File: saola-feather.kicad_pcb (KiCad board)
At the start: 2 copper layers, 27.9 x 53.3 mm, 11 parts, among them J1 Conn_01x21_Female, J2 FeatherTop, J3 Conn_01x04_Male, J4 USB_B_Micro, J5 FeatherBottom, J6 Conn_02x05_Odd_Even, J7 Conn_01x21_Female

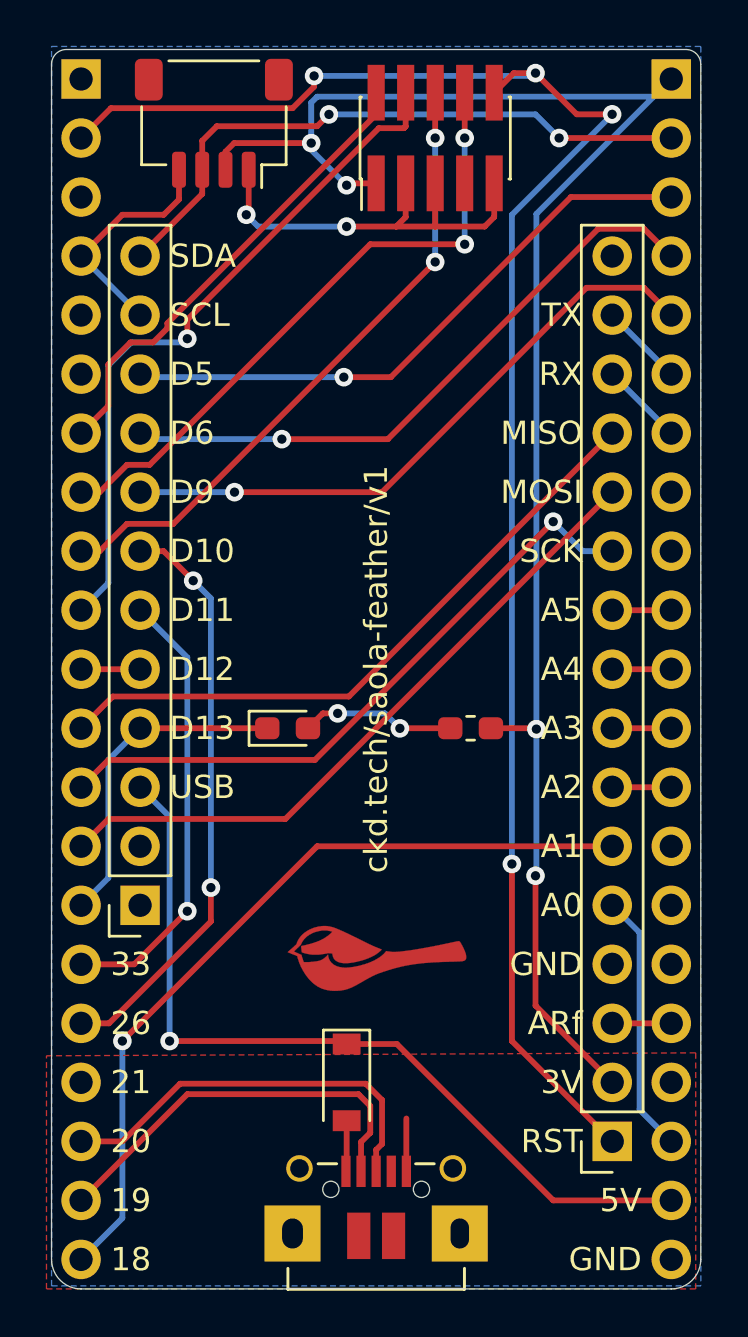
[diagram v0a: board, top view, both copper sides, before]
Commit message: Second version with fixed I2C
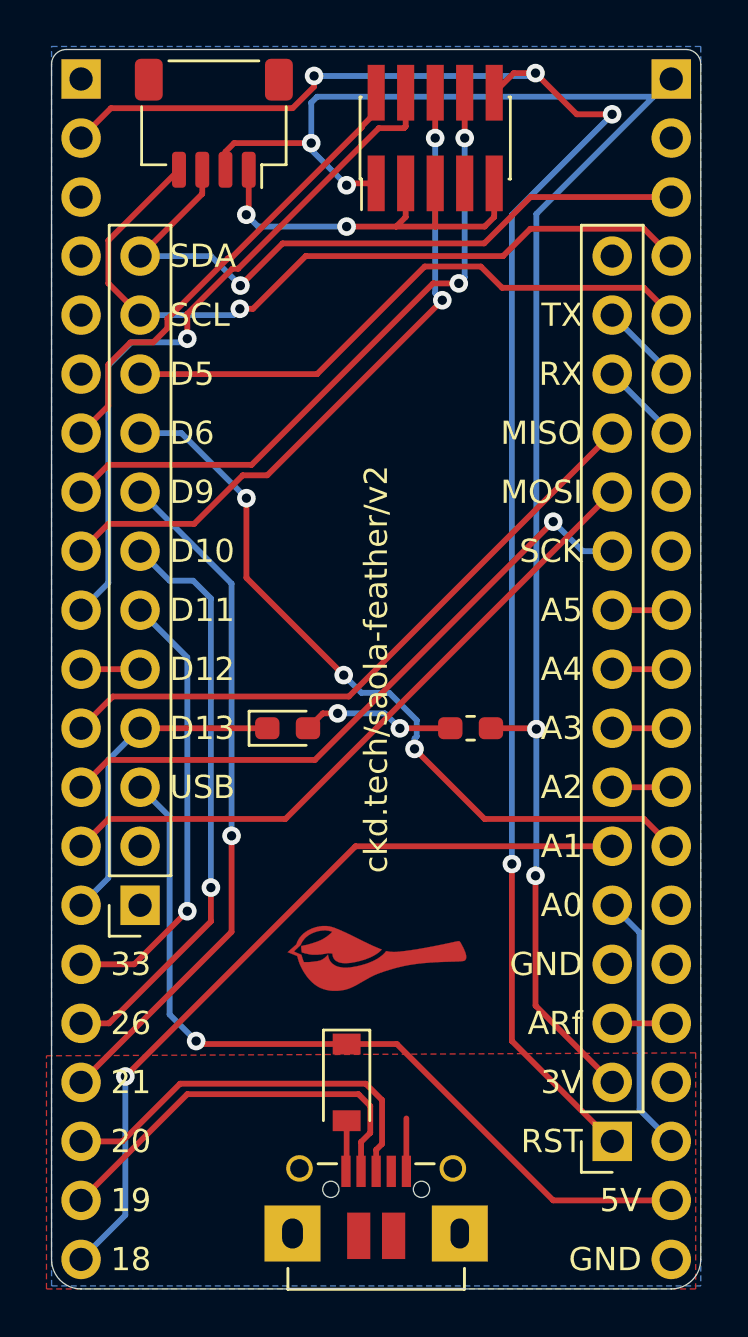
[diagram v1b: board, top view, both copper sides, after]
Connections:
- J2 pad 10: /IO1 -> /IO3
- J2 pad 11: /IO45 -> /IO2
- J2 pad 12: /IO0 -> /IO1
- J2 pad 8: /IO3 -> /IO21
- J2 pad 9: /IO2 -> /IO12
- J3 pad 3: /IO0 -> /IO1
- J3 pad 4: /IO45 -> /IO2
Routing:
- net /IO12: track 0.00 -> 33.5 mm, vias 0 -> 3
- net /IO21: track 0.00 -> 29.7 mm, vias 0 -> 1
- net /IO0: track 27.1 -> 0.00 mm, vias 2 -> 0
- net /IO45: track 10.1 -> 0.00 mm
- net /IO2: track 27.2 -> 33.0 mm
- net /IO1: track 26.1 -> 29.8 mm
- net /TDO_IO40: track 27.7 -> 29.1 mm
- net /IO3: track 27.0 -> 25.8 mm, vias 1 -> 0
- net /IO18: track 34.7 -> 33.7 mm
- net /TDI_IO41: track 27.5 -> 28.3 mm
- net +5V: track 35.9 -> 35.2 mm
- net /IO26: vias 2 -> 1
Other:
- board text added: "ckd.tech/saola-feather/v2"
- board text removed: "ckd.tech/saola-feather/v1"

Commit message: Add RC circuit for reset. V3
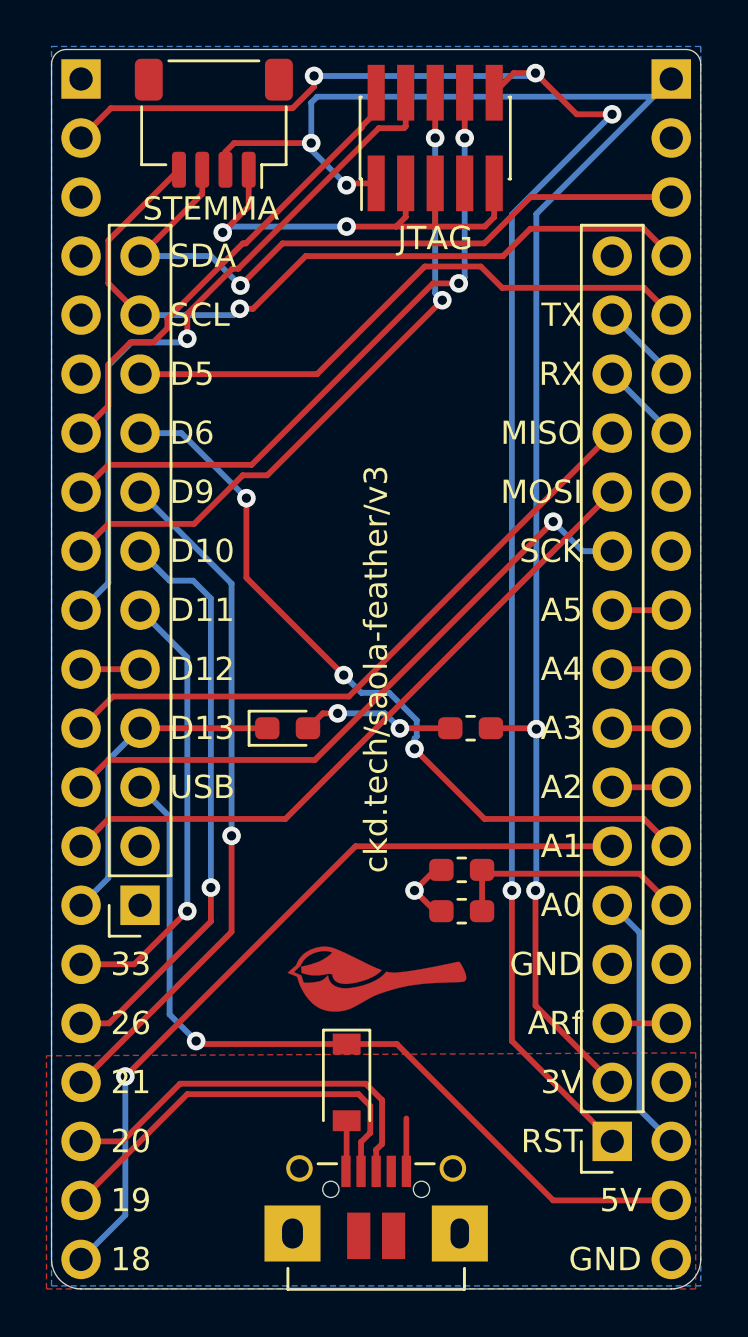
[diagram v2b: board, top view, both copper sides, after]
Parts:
- added C1: 1uF, Capacitor_SMD:C_0603_1608Metric_Pad1.05x0.95mm_HandSolder, F.Cu at (118.0, 110.2)
- added R2: 100k+, Resistor_SMD:R_0603_1608Metric_Pad1.05x0.95mm_HandSolder, F.Cu at (118.0, 112.0)
- moved G*** 0.89 mm to (114.3, 114.9)
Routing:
- net /IO13: track 0.00 -> 10.6 mm
- net GND: track 20.6 -> 25.8 mm, vias 2 -> 3
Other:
- board text added: "JTAG"
- board text added: "STEMMA"
- board text added: "ckd.tech/saola-feather/v3"
- board text removed: "ckd.tech/saola-feather/v2"

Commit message: Tweak pinout:
* D10 is now IO6
* A5 is IO7
* A4 is IO8
* A3 is IO9
* A2 is IO10
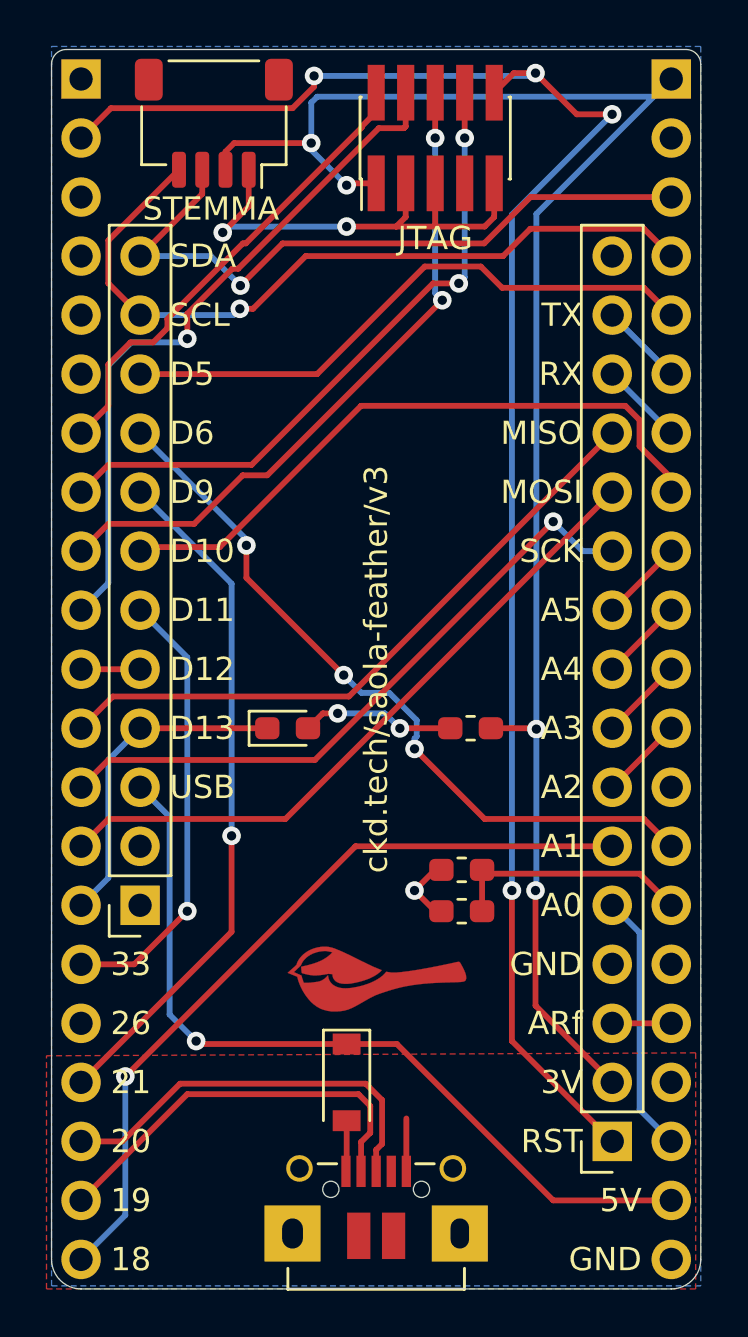
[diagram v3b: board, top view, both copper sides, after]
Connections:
- J2 pad 7: /IO26 -> /IO6
- J5 pad 10: /IO8 -> /IO7
- J5 pad 7: /IO11 -> /IO10
- J5 pad 8: /IO10 -> /IO9
- J5 pad 9: /IO9 -> /IO8
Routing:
- net /IO6: track 0.00 -> 28.0 mm
- net /IO26: track 25.2 -> 0.00 mm, vias 1 -> 0
- net /IO7: track 0.00 -> 3.59 mm
- net /IO11: track 2.54 -> 0.00 mm
- net /IO9: track 2.54 -> 3.59 mm
- net /IO10: track 2.54 -> 3.59 mm
- net /IO8: track 2.54 -> 3.59 mm
- net /IO12: track 33.5 -> 32.4 mm
